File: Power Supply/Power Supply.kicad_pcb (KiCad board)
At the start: 2 copper layers, 40.3 x 104.5 mm, 31 parts, among them J1 Conn_02x08_Odd_Even, SW1 SW_SPDT, U1 LM7812_TO220, U2 LM7912_TO220, U3 LM7805_TO220

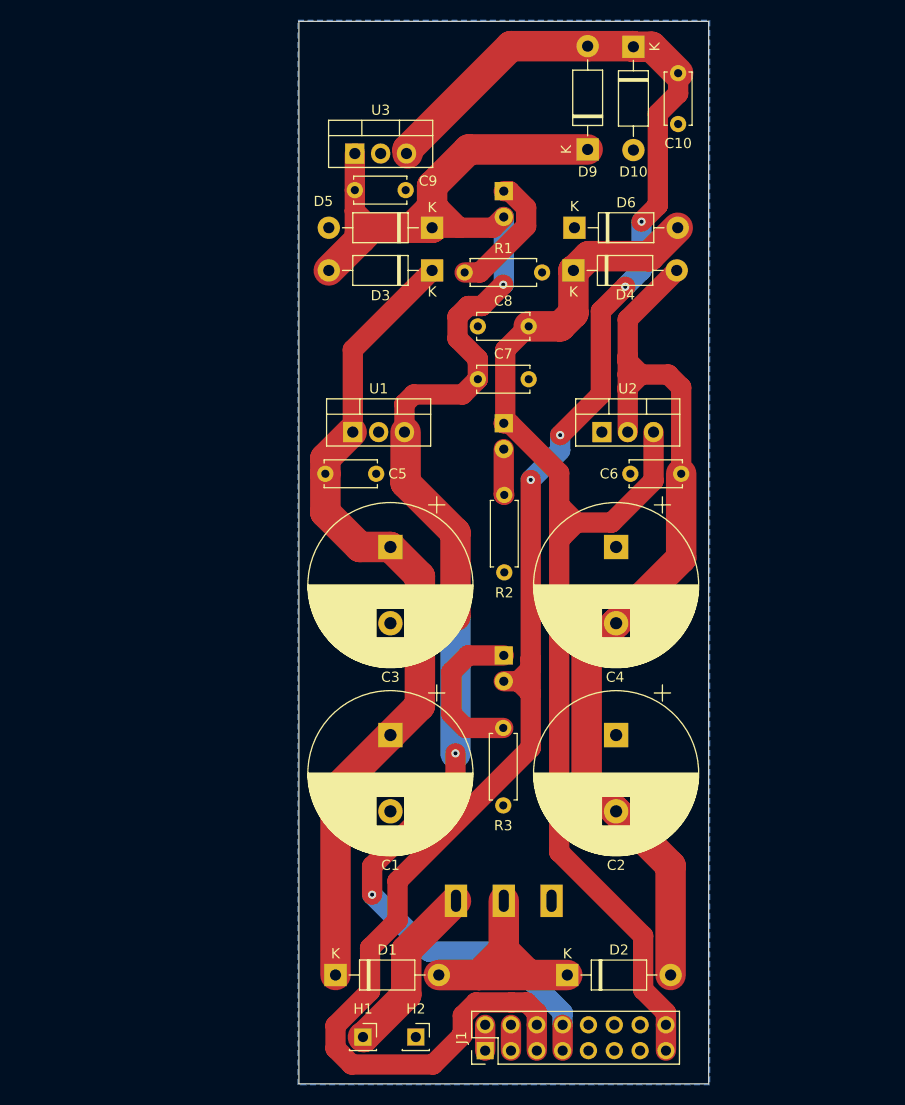
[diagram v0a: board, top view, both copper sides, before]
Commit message: Place PSU components on PCB
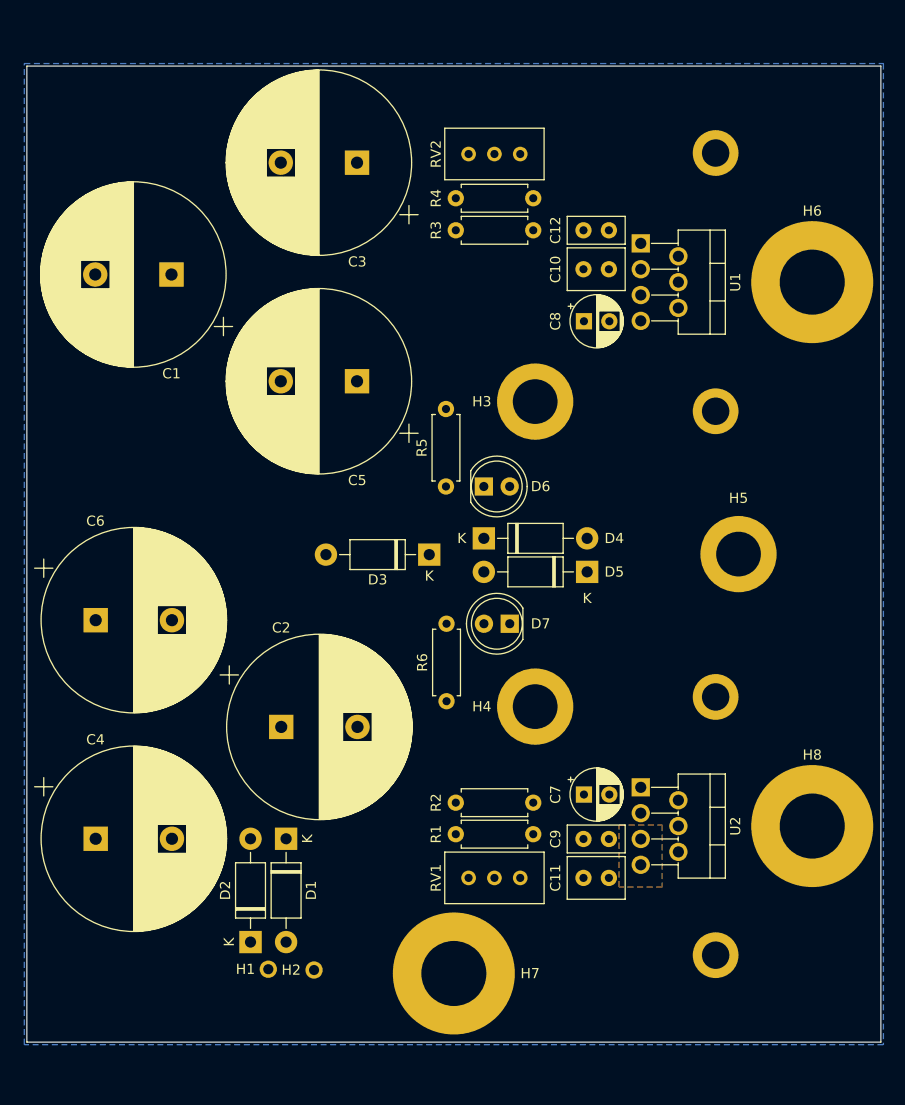
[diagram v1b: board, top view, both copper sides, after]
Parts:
- removed D10, D9: 1N5819, Diode_THT:D_DO-41_SOD81_P10.16mm_Horizontal
- removed D11, D8: LED, LED_THT:LED_D5.0mm
- removed J1: Conn_02x08_Odd_Even, Connector_PinHeader_2.54mm:PinHeader_2x08_P2.54mm_Vertical
- removed SW1: SW_SPDT, Switch:MTS-102_MTS-103_MTS-112_MTS-113_MTS-123
- removed U3: LM7805_TO220, Package_TO_SOT_THT:TO-220-3_Vertical
- added C11: 10u, 0_Capacitor_THT:C_Disc_D5.5mm_W4.0mm_P2.50mm, F.Cu at (159.9, 132.3)
- added C12: 10n, 0_Capacitor_THT:C_Disc_D5.5mm_W2.5mm_P2.50mm, F.Cu at (157.4, 68.7)
- added H3: MNT_STANDOFF, 0_MountingHole:MountingHole_Pitch7.5mm_Drill3.4mm, F.Cu at (152.6, 85.5)
- added H4: MNT_STANDOFF, 0_MountingHole:MountingHole_Pitch7.5mm_Drill3.4mm, F.Cu at (152.6, 115.5)
- added H5: MNT_STANDOFF, 0_MountingHole:MountingHole_Pitch7.5mm_Drill3.4mm, F.Cu at (172.6, 100.5)
- added H6: MNT_12V_POS, 0_MountingHole:MountingHole_Pitch12mm_Drill6.4mm, F.Cu at (179.9, 73.8)
- added H7: MNT_0V, 0_MountingHole:MountingHole_Pitch12mm_Drill6.4mm, F.Cu at (144.6, 141.8)
- added H8: MNT_12V_NEG, 0_MountingHole:MountingHole_Pitch12mm_Drill6.4mm, F.Cu at (179.9, 127.2)
- added R4: 5.6k, Resistor_THT:R_Axial_DIN0207_L6.3mm_D2.5mm_P7.62mm_Horizontal, F.Cu at (144.8, 65.5)
- added R5: 4.7k, Resistor_THT:R_Axial_DIN0207_L6.3mm_D2.5mm_P7.62mm_Horizontal, F.Cu at (143.9, 93.8)
- added R6: 4.7k, Resistor_THT:R_Axial_DIN0207_L6.3mm_D2.5mm_P7.62mm_Horizontal, F.Cu at (143.9, 115.0)
- added RV1: 10k, Potentiometer_THT:Potentiometer_Bourns_3296W_Vertical, F.Cu at (146.1, 132.3)
- added RV2: 10k, Potentiometer_THT:Potentiometer_Bourns_3296W_Vertical, F.Cu at (146.1, 61.1)
- C1, C2, C3, C4: value 2200u -> 4700u; footprint Capacitor_THT:CP_Radial_D16.0mm_P7.50mm -> Capacitor_THT:CP_Radial_D18.0mm_P7.50mm
- C10: value 1u -> 10u; footprint Capacitor_THT:C_Disc_D5.0mm_W2.5mm_P5.00mm -> 0_Capacitor_THT:C_Disc_D5.5mm_W4.0mm_P2.50mm
- C5, C6: value 1u -> 4700u; footprint Capacitor_THT:C_Disc_D5.0mm_W2.5mm_P5.00mm -> Capacitor_THT:CP_Radial_D18.0mm_P7.50mm
- C7, C8: value 1u -> 10u; footprint Capacitor_THT:C_Disc_D5.0mm_W2.5mm_P5.00mm -> Capacitor_THT:CP_Radial_D5.0mm_P2.50mm
- C9: value 1u -> 0.1u; footprint Capacitor_THT:C_Disc_D5.0mm_W2.5mm_P5.00mm -> 0_Capacitor_THT:C_Disc_D5.5mm_W2.5mm_P2.50mm
- D6: value 1N5819 -> LED; footprint Diode_THT:D_DO-41_SOD81_P10.16mm_Horizontal -> LED_THT:LED_D5.0mm
- D7: moved to F.Cu
- H1: value MountingHole_Pad -> MNT_AC_L; footprint Connector_PinSocket_2.54mm:PinSocket_1x01_P2.54mm_Vertical -> 0_MountingHole:MountingHole_Pitch1.7mm_Drill1mm
- H2: value MountingHole_Pad -> MNT_AC_N; footprint Connector_PinSocket_2.54mm:PinSocket_1x01_P2.54mm_Vertical -> 0_MountingHole:MountingHole_Pitch1.7mm_Drill1mm
- R1: value 33k -> 237k
- R2: value 33k -> 5.1k
- R3: value 22k -> 221k
- U1: value LM7812_TO220 -> LT3086ET7; footprint Package_TO_SOT_THT:TO-220-3_Vertical -> 0_Package_TO_SOT_THT:TO-220-7_P2.54x3.7mm_StaggerOdd_Lead3.8mm_Vertical_HeatSink
- U2: value LM7912_TO220 -> LT3091ET7; footprint Package_TO_SOT_THT:TO-220-3_Vertical -> 0_Package_TO_SOT_THT:TO-220-7_P2.54x3.7mm_StaggerOdd_Lead3.8mm_Vertical_HeatSink
- moved C9 68.5 mm to (159.9, 128.5), turned to 180 degrees
- moved C4 58.7 mm to (109.4, 128.5), turned to 0 degrees
- moved R1 55.7 mm to (152.4, 128.1), turned to 180 degrees
- moved C6 54.5 mm to (109.4, 107.0)
- moved C1 50.2 mm to (116.9, 73.0), turned to 180 degrees
- moved R3 49.0 mm to (152.4, 68.7), turned to 180 degrees
- moved D7 42.6 mm to (150.1, 107.3), turned to 180 degrees
- moved C7 42.2 mm to (157.4, 124.2)
- moved C3 37.9 mm to (135.1, 62.0), turned to 180 degrees
- moved D5 37.1 mm to (157.8, 102.2)
- moved U2 35.2 mm to (163.0, 123.5), turned to -90 degrees
- moved U1 33.9 mm to (163.0, 70.0), turned to -90 degrees
- moved C2 32.9 mm to (127.7, 117.5), turned to 0 degrees
- moved D2 31.3 mm to (124.6, 138.7), turned to 90 degrees
- moved D3 28.0 mm to (142.2, 100.5)
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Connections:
- C10 pad 1: +5V -> +12V
- C7 pad 1: +12V -> GND
- C7 pad 2: GND -> Net-(C2-Pad2)
- C8 pad 2: -12V -> Net-(C1-Pad1)
- C9 pad 1: +12V -> Net-(C9-Pad1)
- D3 pad 1: Net-(C1-Pad1) -> -12V
- D3 pad 2: +12V -> Net-(C2-Pad2)
- D4 pad 1: -12V -> +12V
- D4 pad 2: Net-(C2-Pad2) -> GND
- D5 pad 1: +12V -> GND
- D5 pad 2: GND -> -12V
- D6 pad 1: GND -> Net-(D6-Pad1)
- D6 pad 2: -12V -> +12V
- D7 pad 1: Net-(D7-Pad1) -> -12V
- D7 pad 2: +12V -> Net-(D7-Pad2)
- H1 pad 1: AC -> Net-(D1-Pad2)
- R1 pad 1: Net-(D7-Pad1) -> Net-(C9-Pad1)
- R1 pad 2: GND -> Net-(R1-Pad2)
- R2 pad 1: GND -> Net-(C2-Pad2)
- R2 pad 2: Net-(D8-Pad2) -> Net-(R2-Pad2)
- R3 pad 1: Net-(D11-Pad1) -> +12V
- R3 pad 2: GND -> Net-(R3-Pad2)
- U1 pad 1: Net-(C1-Pad1) -> GND
- U1 pad 2: GND -> Net-(C12-Pad2)
- U2 pad 1: GND -> Net-(R2-Pad2)
- U2 pad 2: Net-(C2-Pad2) -> GND
- U2 pad 3: -12V -> Net-(C2-Pad2)
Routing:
- net +5V: track 176.3 -> 0.00 mm, vias 4 -> 0
- net +12V: track 166.9 -> 0.00 mm, vias 4 -> 0
- net -12V: track 120.9 -> 0.00 mm
- net Net-(C2-Pad2): track 93.1 -> 0.00 mm
- net Net-(C1-Pad1): track 82.7 -> 0.00 mm
- net Net-(D1-Pad2): track 24.4 -> 0.00 mm
- net AC: track 17.2 -> 0.00 mm
- net Net-(D11-Pad1): track 15.6 -> 0.00 mm
- net Net-(D7-Pad1): track 12.6 -> 0.00 mm
- net Net-(D8-Pad2): track 4.53 -> 0.00 mm
- net Net-(J1-Pad3): track 2.54 -> 0.00 mm
- net Net-(J1-Pad1): track 2.54 -> 0.00 mm
- added copper zone on B.Cu, net -12V
- added copper zone on F.Cu, net -12V
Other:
- board size 40.3 x 104.5 mm -> 84 x 96 mm
- net class Default removed

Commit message: Begin routing PSU, upgrade to KiCad 7
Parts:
- moved RV2 16.8 mm to (147.3, 77.9)
- moved C12 4.69 mm to (160.1, 72.5), turned to 90 degrees
- moved C10 4.45 mm to (156.2, 70.0), turned to -90 degrees
- moved R3 4.16 mm to (152.3, 72.8), turned to 90 degrees
- moved H2 3.11 mm to (134.0, 141.4)
- moved R4 2.45 mm to (147.3, 65.2), turned to -90 degrees
- moved D1 2.36 mm to (130.5, 128.4)
- moved H1 1.50 mm to (127.9, 141.3)
- moved D2 0.62 mm to (125.2, 138.6)
- moved C8 0.06 mm to (157.5, 77.6)
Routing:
- net Net-(C1-Pad1): track 0.00 -> 152.0 mm
- net Net-(C2-Pad2): track 0.00 -> 96.6 mm
- net Net-(C12-Pad2): track 0.00 -> 35.8 mm
- net +12V: track 0.00 -> 17.3 mm
- net Net-(D1-Pad2): track 0.00 -> 12.9 mm
- net Net-(R4-Pad2): track 0.00 -> 5.10 mm
- net Net-(R3-Pad2): track 0.00 -> 5.04 mm

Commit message: Fix DRC issues
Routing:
- net Net-(U1-SET): track 35.8 -> 44.6 mm
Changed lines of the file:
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@@
     (property "ki_description" "Mounting Hole with connection")
     (property "ki_keywords" "mounting hole")
-    (attr smd)
+    (attr through_hole)
     (fp_text reference "H5" (at 0 -5.5 unlocked) (layer "F.SilkS")
         (effects (font (size 1 1) (thickness 0.15)))
@@
     (property "ki_keywords" "cap capacitor")
     (attr through_hole)
-    (fp_text reference "C12" (at -2.75 0) (layer "F.SilkS")
+    (fp_text reference "C12" (at 5.18 0) (layer "F.SilkS")
         (effects (font (size 1 1) (thickness 0.15)))
     )
@@
     (property "ki_description" "Mounting Hole with connection")
     (property "ki_keywords" "mounting hole")
-    (attr smd)
+    (attr through_hole)
     (fp_text reference "H7" (at 7.5 0 unlocked) (layer "F.SilkS")
         (effects (font (size 1 1) (thickness 0.15)))
@@
     (property "ki_description" "Mounting Hole with connection")
     (property "ki_keywords" "mounting hole")
-    (attr smd)
+    (attr through_hole)
     (fp_text reference "H4" (at -5.25 0 unlocked) (layer "F.SilkS")
         (effects (font (size 1 1) (thickness 0.15)))
@@
     (property "ki_description" "Mounting Hole with connection")
     (property "ki_keywords" "mounting hole")
-    (attr smd)
+    (attr through_hole)
     (fp_text reference "H8" (at 0 -7 unlocked) (layer "F.SilkS")
         (effects (font (size 1 1) (thickness 0.15)))
@@
     (property "ki_keywords" "cap capacitor")
     (attr through_hole)
-    (fp_text reference "C10" (at 5.25 -0.02) (layer "F.SilkS")
+    (fp_text reference "C10" (at -2.7 0) (layer "F.SilkS")
         (effects (font (size 1 1) (thickness 0.15)))
     )
@@
     (property "ki_keywords" "cap capacitor")
     (attr through_hole)
-    (fp_text reference "C8" (at -2.794888 0 90) (layer "F.SilkS")
+    (fp_text reference "C8" (at 1.205112 3.7 180) (layer "F.SilkS")
         (effects (font (size 1 1) (thickness 0.15)))
     )
@@
     (property "ki_description" "Mounting Hole with connection")
     (property "ki_keywords" "mounting hole")
-    (attr smd)
+    (attr through_hole)
     (fp_text reference "H6" (at 0 -7 unlocked) (layer "F.SilkS")
         (effects (font (size 1 1) (thickness 0.15)))
@@
     (property "ki_description" "Mounting Hole with connection")
     (property "ki_keywords" "mounting hole")
-    (attr smd)
+    (attr through_hole)
     (fp_text reference "H3" (at -5.25 0 unlocked) (layer "F.SilkS")
         (effects (font (size 1 1) (thickness 0.15)))
@@
   (segment (start 166.45 80.05) (end 169.175 77.325) (width 2.25) (layer "F.Cu") (net 7))
   (segment (start 152.34 77.9) (end 154.49 80.05) (width 2.25) (layer "F.Cu") (net 7))
-  (segment (start 166.725 71.21) (end 166.725 69.19) (width 2.25) (layer "F.Cu") (net 7))
-  (segment (start 166.725 70.025) (end 167.91 71.21) (width 2.25) (layer "F.Cu") (net 7))
+  (segment (start 166.725 69.025) (end 166.725 71.21) (width 2) (layer "F.Cu") (net 7))
+  (segment (start 167.91 70.21) (end 167.91 71.21) (width 2) (layer "F.Cu") (net 7))
   (segment (start 167.91 71.21) (end 166.725 71.21) (width 2.25) (layer "F.Cu") (net 7))
   (segment (start 154.49 80.05) (end 166.45 80.05) (width 2.25) (layer "F.Cu") (net 7))
-  (segment (start 166.725 69.19) (end 165.25 67.715) (width 2.25) (layer "F.Cu") (net 7))
+  (segment (start 160.965 67.8) (end 165.5 67.8) (width 2) (layer "F.Cu") (net 7))
+  (segment (start 160.1 69.98) (end 160.1 68.665) (width 2) (layer "F.Cu") (net 7))
   (segment (start 149.8 77.9) (end 152.34 77.9) (width 2.25) (layer "F.Cu") (net 7))
   (segment (start 169.175 72.475) (end 167.91 71.21) (width 2.25) (layer "F.Cu") (net 7))
-  (segment (start 166.725 69.19) (end 166.725 70.025) (width 2.25) (layer "F.Cu") (net 7))
+  (segment (start 165.5 67.8) (end 166.725 69.025) (width 2) (layer "F.Cu") (net 7))
   (segment (start 169.175 77.325) (end 169.175 72.475) (width 2.25) (layer "F.Cu") (net 7))
+  (segment (start 165.5 67.8) (end 167.91 70.21) (width 2) (layer "F.Cu") (net 7))
+  (segment (start 160.1 68.665) (end 160.965 67.8) (width 2) (layer "F.Cu") (net 7))
   (segment (start 125.25 138.58) (end 125.25 138.69) (width 4) (layer "F.Cu") (net 8))
   (segment (start 125.25 138.58) (end 130.5 138.58) (width 4) (layer "F.Cu") (net 8))

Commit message: Finish routing
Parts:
- moved R2 3.35 mm to (144.8, 121.6)
- moved R1 0.25 mm to (152.4, 127.8)
- moved RV1 0.25 mm to (146.1, 132.1)
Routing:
- net Net-(D2-A): track 96.6 -> 169.8 mm
- net +12V: track 17.3 -> 40.6 mm
- net -12V: track 0.00 -> 23.2 mm
- net Net-(U2-SET): track 0.00 -> 12.3 mm
- net Net-(U2-ILIM): track 0.00 -> 11.3 mm
- net Net-(R1-Pad2): track 0.00 -> 4.82 mm
- net Net-(D6-K): track 0.00 -> 3.72 mm
- net Net-(D7-A): track 0.00 -> 3.68 mm
- added copper zone on F.Cu, net +12V

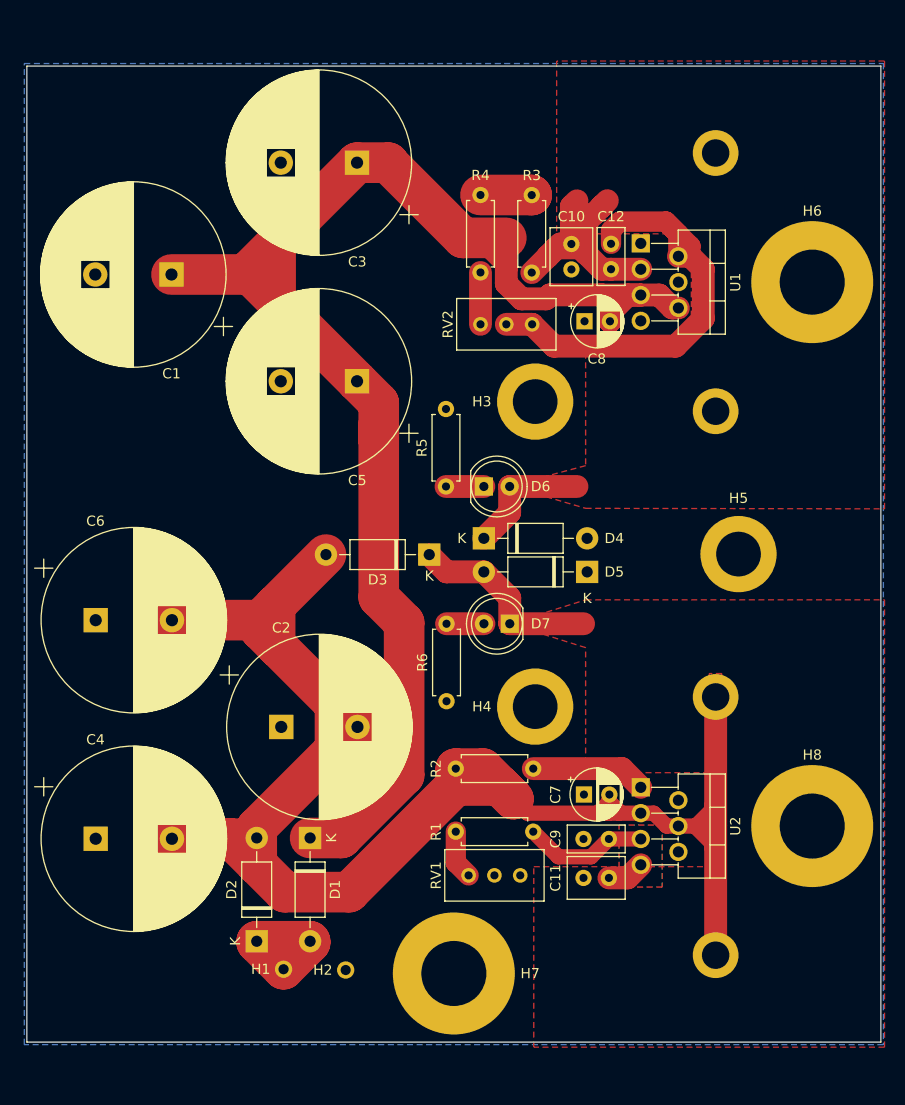
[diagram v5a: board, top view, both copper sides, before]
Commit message: Create additional filled zones
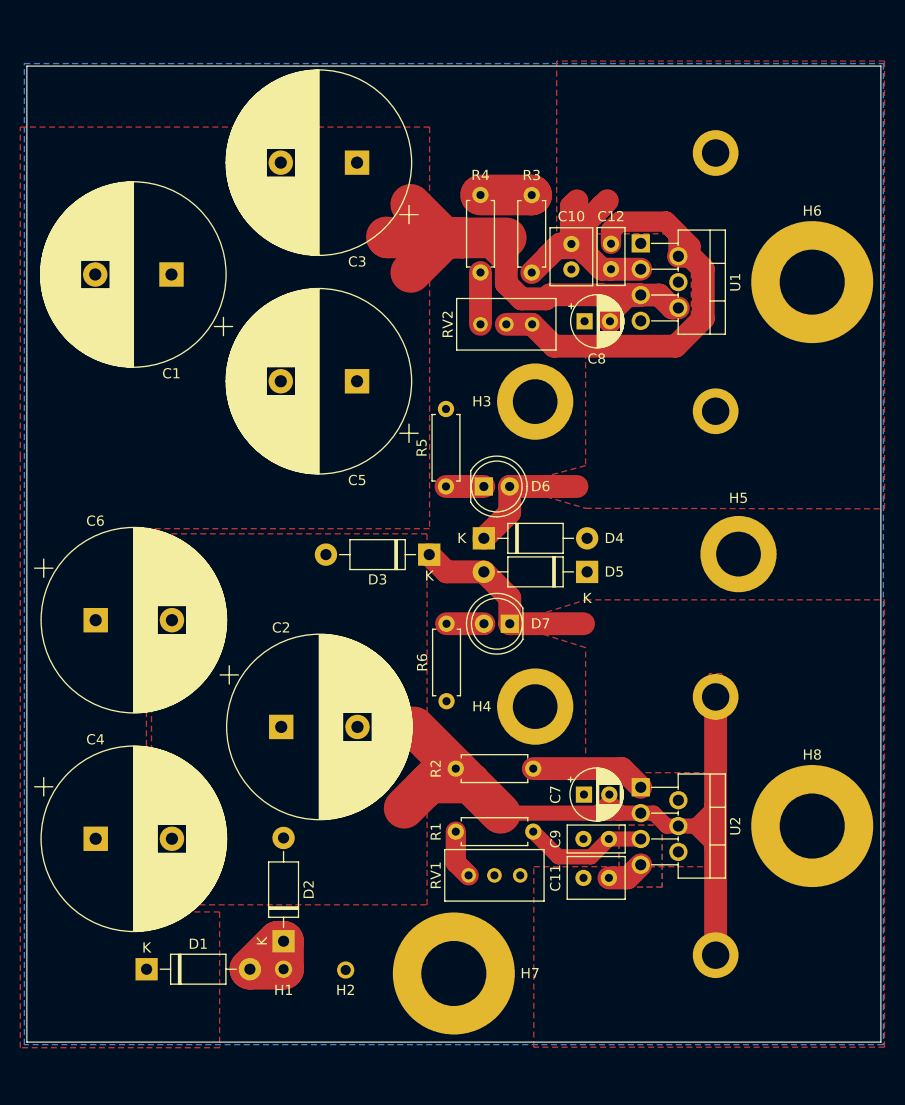
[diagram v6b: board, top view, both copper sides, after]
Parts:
- moved D1 20.6 mm to (114.4, 141.3), turned to 0 degrees
- moved D2 2.64 mm to (127.9, 138.6)
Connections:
- net Net-(D1-K) renamed AC_REC_P
- net Net-(D2-A) renamed AC_REC_N
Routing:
- net AC_REC_P: track 152.0 -> 59.6 mm
- net AC_REC_N: track 169.8 -> 81.9 mm
- net Net-(D1-A): track 12.9 -> 10.5 mm
- added copper zone on F.Cu, net AC_REC_N
- added copper zone on F.Cu, net AC_REC_P
